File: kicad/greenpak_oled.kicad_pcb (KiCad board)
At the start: 2 copper layers, 35.6 x 35.6 mm, 21 parts, among them J1 Conn_01x05_Pin, J3 POGO_SOCKET, U1 SLG46826G, U2 OLED-128O064D

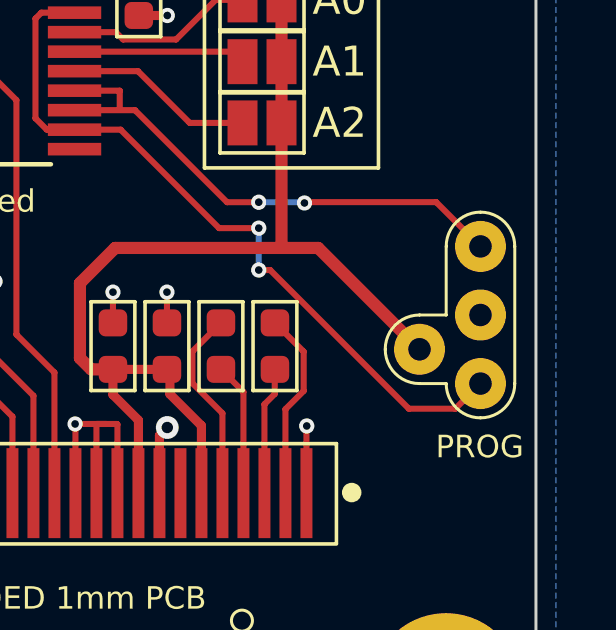
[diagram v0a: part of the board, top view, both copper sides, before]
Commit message: Updated pogo socket dimensions.
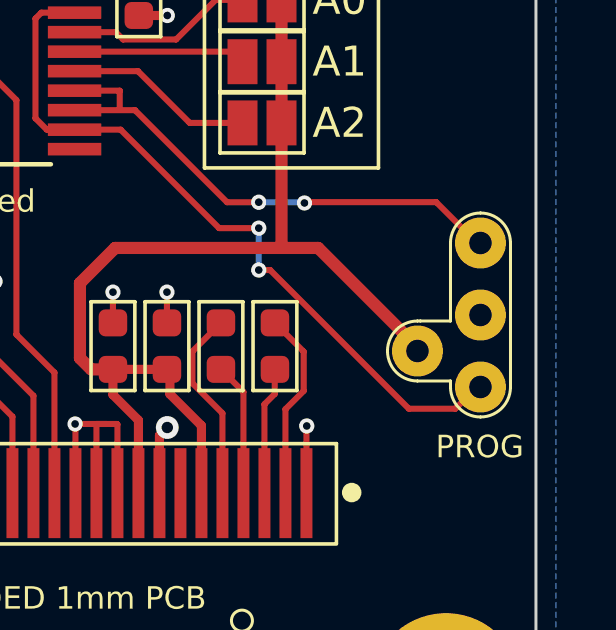
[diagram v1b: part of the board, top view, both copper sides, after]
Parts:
- J3: footprint greenpak_oled:POGO_SOCKET -> greenpak_oled:GREENPAK_POGO_SOCKET
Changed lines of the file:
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@@
     )
   )
-  (footprint "greenpak_oled:POGO_SOCKET" locked (layer "F.Cu")
+  (footprint "greenpak_oled:GREENPAK_POGO_SOCKET" locked (layer "F.Cu")
     (at 15.9512 2.3622 90)
     (descr "Through hole straight pin header, 1x01, 2.54mm pitch, single row")
@@
         (effects (font (size 1 1) (thickness 0.15)))
     )
-    (fp_line (start -3.429 0) (end -3.429 0)
+    (fp_line (start -3.4 0) (end -3.4 0)
       (stroke (width 0.1) (type default)) (layer "F.SilkS"))
-    (fp_line (start -2.286 -2.032) (end -2.286 -1.143)
+    (fp_line (start -2.4 -1) (end -2.2 -1)
       (stroke (width 0.1) (type default)) (layer "F.SilkS"))
-    (fp_line (start -2.286 -1.143) (end -2.286 -1.143)
+    (fp_line (start -2.2 -1) (end -2.2 -2.1)
       (stroke (width 0.1) (type default)) (layer "F.SilkS"))
-    (fp_line (start -2.286 1.143) (end 2.286 1.143)
+    (fp_line (start -1.2 -3.1) (end -1.2 -3.1)
       (stroke (width 0.1) (type default)) (layer "F.SilkS"))
-    (fp_line (start -1.143 -3.175) (end -1.143 -3.175)
+    (fp_line (start -0.2 -2.1) (end -0.2 -2)
       (stroke (width 0.1) (type default)) (layer "F.SilkS"))
-    (fp_line (start 0 -1.143) (end 0 -2.032)
+    (fp_line (start -0.2 -1) (end -0.2 -2)
       (stroke (width 0.1) (type default)) (layer "F.SilkS"))
-    (fp_line (start 2.286 -1.143) (end 0 -1.143)
+    (fp_line (start -0.2 -1) (end 2.4 -1)
       (stroke (width 0.1) (type default)) (layer "F.SilkS"))
-    (fp_line (start 3.429 0) (end 3.429 0)
+    (fp_line (start 2.4 1) (end -2.4 1)
       (stroke (width 0.1) (type default)) (layer "F.SilkS"))
-    (fp_arc (start -3.429 0) (mid -3.094223 -0.808223) (end -2.286 -1.143)
+    (fp_line (start 3.4 0) (end 3.4 0)
       (stroke (width 0.1) (type default)) (layer "F.SilkS"))
-    (fp_arc (start -2.286 -2.032) (mid -1.951223 -2.840223) (end -1.143 -3.175)
+    (fp_arc (start -3.4 0) (mid -3.107107 -0.707107) (end -2.4 -1)
       (stroke (width 0.1) (type default)) (layer "F.SilkS"))
-    (fp_arc (start -2.286 1.143) (mid -3.094223 0.808223) (end -3.429 0)
+    (fp_arc (start -2.4 1) (mid -3.107107 0.707107) (end -3.4 0)
       (stroke (width 0.1) (type default)) (layer "F.SilkS"))
-    (fp_arc (start -1.143 -3.175) (mid -0.334777 -2.840223) (end 0 -2.032)
+    (fp_arc (start -2.2 -2.1) (mid -1.907107 -2.807107) (end -1.2 -3.1)
       (stroke (width 0.1) (type default)) (layer "F.SilkS"))
-    (fp_arc (start 2.286 -1.143) (mid 3.094223 -0.808223) (end 3.429 0)
+    (fp_arc (start -1.2 -3.1) (mid -0.492893 -2.807107) (end -0.2 -2.1)
       (stroke (width 0.1) (type default)) (layer "F.SilkS"))
-    (fp_arc (start 3.429 0) (mid 3.094223 0.808223) (end 2.286 1.143)
+    (fp_arc (start 2.4 -1) (mid 3.107107 -0.707107) (end 3.4 0)
       (stroke (width 0.1) (type default)) (layer "F.SilkS"))
-    (pad "1" thru_hole circle locked (at -2.286 0 90) (size 1.7 1.7) (drill 0.75) (layers "*.Cu" "F.Mask")
+    (fp_arc (start 3.4 0) (mid 3.107107 0.707107) (end 2.4 1)
+      (stroke (width 0.1) (type default)) (layer "F.SilkS"))
+    (pad "1" thru_hole circle locked (at -2.4 0 90) (size 1.7 1.7) (drill 0.75) (layers "*.Cu" "F.Mask")
       (net 12 "Net-(J3-SDA)") (pinfunction "SDA") (pintype "passive"))
     (pad "2" thru_hole circle locked (at 0 0 90) (size 1.7 1.7) (drill 0.75) (layers "*.Cu" "F.Mask")
       (net 2 "GND") (pinfunction "GND") (pintype "passive"))
-    (pad "3" thru_hole circle locked (at 2.286 0 90) (size 1.7 1.7) (drill 0.75) (layers "*.Cu" "F.Mask")
+    (pad "3" thru_hole circle locked (at 2.4 0 90) (size 1.7 1.7) (drill 0.75) (layers "*.Cu" "F.Mask")
       (net 13 "Net-(J3-SCL)") (pinfunction "SCL") (pintype "passive"))
-    (pad "4" thru_hole circle locked (at -1.143 -2.032 90) (size 1.7 1.7) (drill 0.75) (layers "*.Cu" "F.Mask")
+    (pad "4" thru_hole circle locked (at -1.2 -2.1 90) (size 1.7 1.7) (drill 0.75) (layers "*.Cu" "F.Mask")
       (net 1 "VDD") (pinfunction "VCC") (pintype "passive"))
+    (group "" (id 9a20962a-96cb-444c-b769-105f3744111a)
+      (members
+        0fb24245-a20f-439a-a7a6-482a1eeed57c
+        704a574d-164b-437e-b665-32adf99cf937
+        7156aa13-4481-4be6-91ec-9592edb7d8ef
+        78b20d77-63b2-40b4-8e6c-6dafab391901
+        7b7e2a12-cb9f-4923-911c-0050bdd448e5
+        93738706-9cc0-494d-bd40-c0bdb8bd095c
+        a79de5ce-e2f1-4ce7-98d3-5de9269a25e3
+        a90e6c7f-038d-4d69-85c5-f695cbc771de
+        b19a07be-eb56-49ff-af96-73dbf4c76579
+        cb01a863-af4a-4586-b96f-5acbf13591f6
+        d395e180-3a52-4205-93dc-61c1b6c8868b
+        d7b9f1a4-8c7d-4224-b90c-e13095c5ed81
+        db9aa40e-af5e-419d-8627-f1f7f49816c7
+        f6330e70-d4a1-4cca-942c-1e832035a826
+        f983e5a0-8cb4-4e4c-b24f-1f5db3c54be6
+      )
+    )
   )
   (footprint "greenpak_oled:PinHeader_1x05_P2.54mm_Vertical" (layer "F.Cu")
